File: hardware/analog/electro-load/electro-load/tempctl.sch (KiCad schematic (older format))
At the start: 28 parts, among them M1 Noctua NF-A14 5V, Q1 2N2222A, Q2 2N2222A, U12 LMV321, U13 LMV321

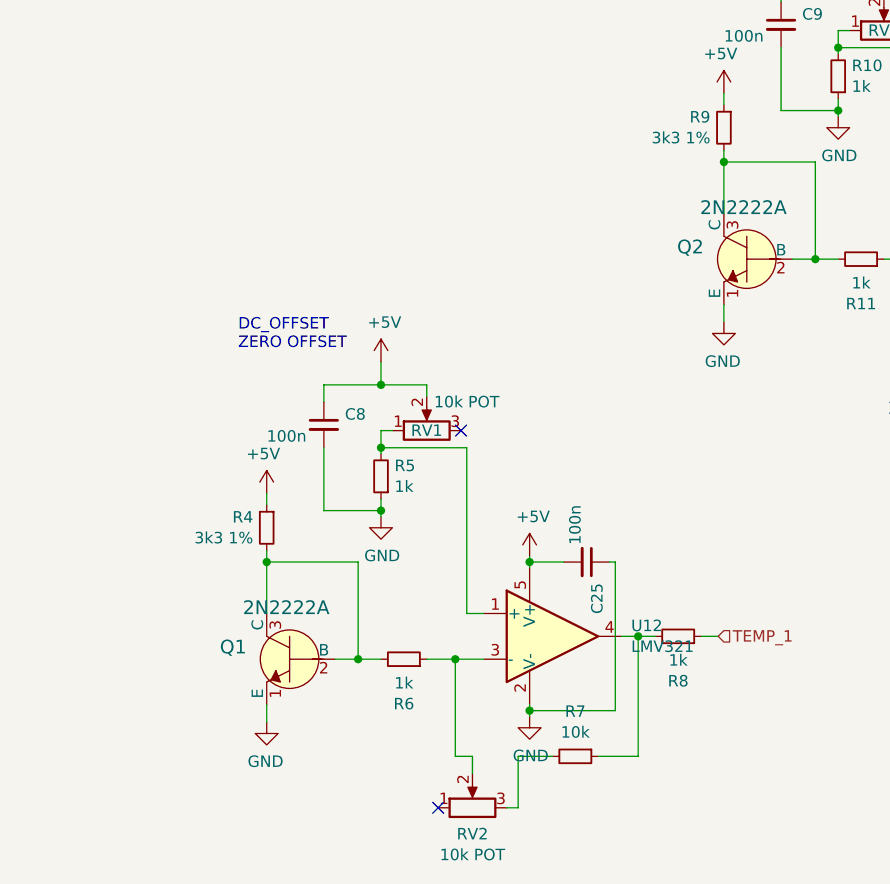
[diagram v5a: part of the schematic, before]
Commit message: Added extra footprints for temperature probes - 2N4921
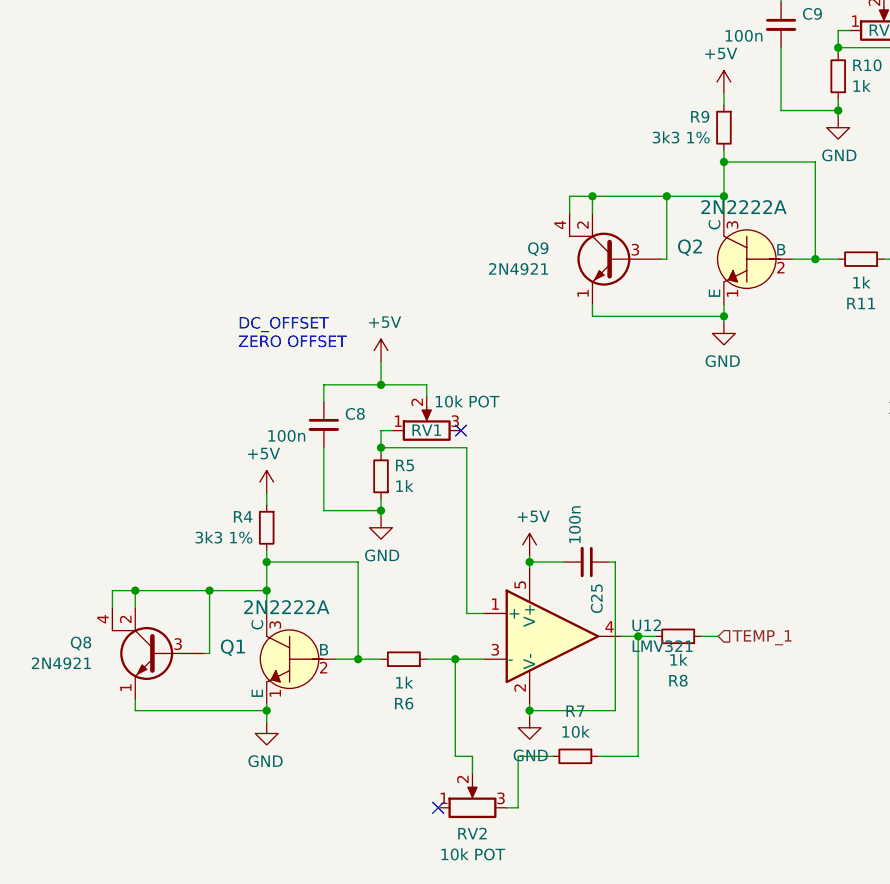
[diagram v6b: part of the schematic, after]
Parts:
- added Q8, Q9: 2N4921, Package_TO_SOT_THT:TO-126-3_Vertical, symbol Device:Q_NPN_ECBC
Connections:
- net GND: now also Q8.1 (E), Q9.1 (E)
- net at Q2.2 (B), Q2.3 (C), R11.2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: now also Q9.2 (C), Q9.3 (B), Q9.4 (C)
- net at Q1.2 (B), Q1.3 (C), R4.2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: now also Q8.2 (C), Q8.3 (B), Q8.4 (C)
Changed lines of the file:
@@
 $EndComp
 Wire Wire Line
-	3700 4475 3700 4250
+	3700 4475 3700 4400
 Wire Wire Line
 	3700 4250 4100 4250
@@
 $EndComp
 Wire Wire Line
-	3700 4950 3700 4875
+	3700 4950 3700 4925
 $Comp
 L Device:R_Small R?
@@
 $EndComp
 Wire Wire Line
-	1700 6225 1700 6000
+	1700 6225 1700 6125
 Wire Wire Line
 	1700 6000 2100 6000
@@
 $EndComp
 Wire Wire Line
-	1700 6700 1700 6625
+	1700 6700 1700 6650
 $Comp
 L Device:R_Small R?
@@
 	0    1    -1   0
 $EndComp
+$Comp
+L Device:Q_NPN_ECBC Q9
+U 1 1 5EA5BCE1
+P 3225 4675
+F 0 "Q9" H 3513 4721 50  0000 L CNN
+F 1 "2N4921" H 3513 4630 50  0000 L CNN
+F 2 "Package_TO_SOT_THT:TO-126-3_Vertical" H 3425 4775 50  0001 C CNN
+F 3 "~" H 3225 4675 50  0001 C CNN
+	1    3225 4675
+	-1   0    0    -1
+$EndComp
+Wire Wire Line
+	3425 4675 3450 4675
+Wire Wire Line
+	3450 4675 3450 4400
+Wire Wire Line
+	3450 4400 3125 4400
+Wire Wire Line
+	3125 4400 3125 4475
+Wire Wire Line
+	3025 4475 3025 4400
+Wire Wire Line
+	3025 4400 3125 4400
+Connection ~ 3125 4400
+Wire Wire Line
+	3450 4400 3700 4400
+Connection ~ 3450 4400
+Connection ~ 3700 4400
+Wire Wire Line
+	3700 4400 3700 4250
+Wire Wire Line
+	3125 4875 3125 4925
+Wire Wire Line
+	3125 4925 3700 4925
+Connection ~ 3700 4925
+Wire Wire Line
+	3700 4925 3700 4875
+$Comp
+L Device:Q_NPN_ECBC Q8
+U 1 1 5EA75838
+P 1225 6400
+F 0 "Q8" H 1513 6446 50  0000 L CNN
+F 1 "2N4921" H 1513 6355 50  0000 L CNN
+F 2 "Package_TO_SOT_THT:TO-126-3_Vertical" H 1425 6500 50  0001 C CNN
+F 3 "~" H 1225 6400 50  0001 C CNN
+	1    1225 6400
+	-1   0    0    -1
+$EndComp
+Wire Wire Line
+	1425 6400 1450 6400
+Wire Wire Line
+	1450 6400 1450 6125
+Wire Wire Line
+	1450 6125 1125 6125
+Wire Wire Line
+	1125 6125 1125 6200
+Wire Wire Line
+	1025 6200 1025 6125
+Wire Wire Line
+	1025 6125 1125 6125
+Connection ~ 1125 6125
+Wire Wire Line
+	1450 6125 1700 6125
+Connection ~ 1450 6125
+Wire Wire Line
+	1125 6600 1125 6650
+Wire Wire Line
+	1125 6650 1700 6650
+Connection ~ 1700 6125
+Wire Wire Line
+	1700 6125 1700 6000
+Connection ~ 1700 6650
+Wire Wire Line
+	1700 6650 1700 6625
 $EndSCHEMATC
